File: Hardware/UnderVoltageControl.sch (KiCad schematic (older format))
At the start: 8 parts

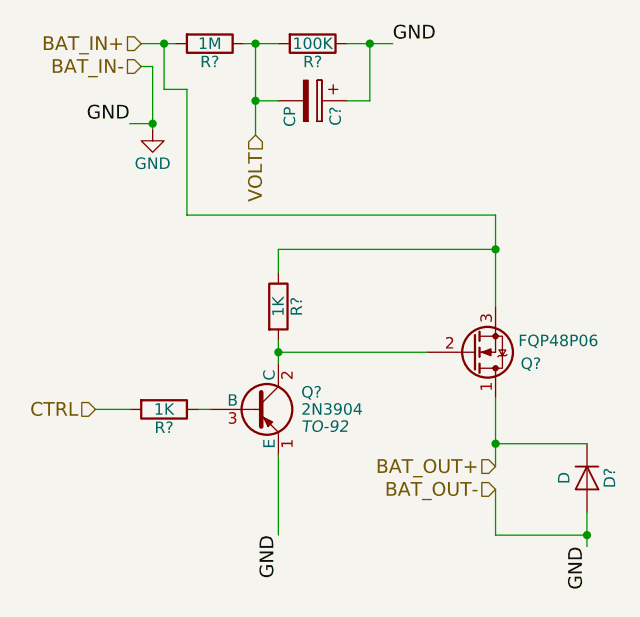
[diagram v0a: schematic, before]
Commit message: Add receiver component
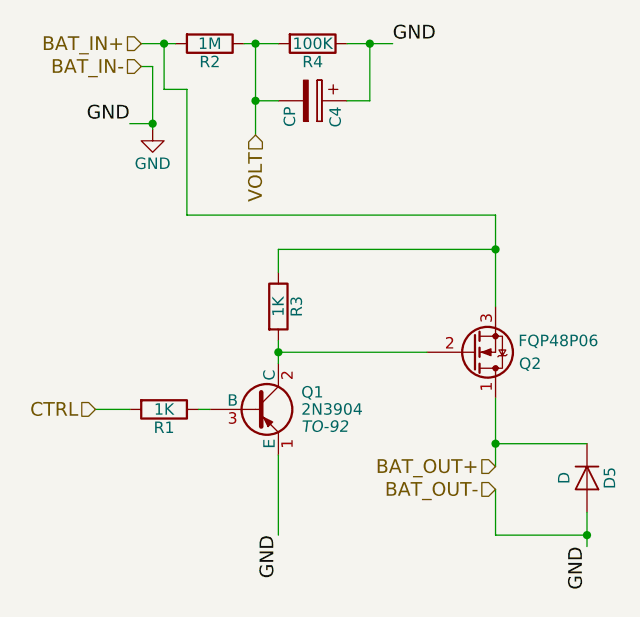
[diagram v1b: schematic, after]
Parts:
- gave numbers to parts that had none: 8
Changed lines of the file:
@@
 LIBS:valves
 LIBS:arduino
-LIBS:RC_Car_Manager-cache
+LIBS:RC_CAR
 EELAYER 25 0
 EELAYER END
@@
 $EndDescr
 $Comp
-L R R?
+L R R2
 U 1 1 5A34D119
 P 4775 2475
-F 0 "R?" V 4855 2475 50  0000 C CNN
+F 0 "R2" V 4855 2475 50  0000 C CNN
 F 1 "1M" V 4775 2475 50  0000 C CNN
 F 2 "" V 4705 2475 50  0000 C CNN
@@
 $EndComp
 $Comp
-L R R?
+L R R4
 U 1 1 5A34D120
 P 5225 2475
-F 0 "R?" V 5305 2475 50  0000 C CNN
+F 0 "R4" V 5305 2475 50  0000 C CNN
 F 1 "100K" V 5225 2475 50  0000 C CNN
 F 2 "" V 5155 2475 50  0000 C CNN
@@
 $EndComp
 $Comp
-L CP C?
+L CP C4
 U 1 1 5A34D127
 P 5225 2725
-F 0 "C?" H 5250 2825 50  0000 L CNN
+F 0 "C4" H 5250 2825 50  0000 L CNN
 F 1 "CP" H 5250 2625 50  0000 L CNN
 F 2 "" H 5263 2575 50  0000 C CNN
@@
 $EndComp
 $Comp
-L GND #PWR?
+L GND #PWR8
 U 1 1 5A34D12E
 P 4525 2850
-F 0 "#PWR?" H 4525 2600 50  0001 C CNN
+F 0 "#PWR8" H 4525 2600 50  0001 C CNN
 F 1 "GND" H 4525 2700 50  0000 C CNN
 F 2 "" H 4525 2850 50  0000 C CNN
@@
 Connection ~ 4975 2725
 $Comp
-L 2SA1016 Q?
+L 2SA1016 Q1
 U 1 1 5A34D145
 P 4975 4075
-F 0 "Q?" H 5175 4150 50  0000 L CNN
+F 0 "Q1" H 5175 4150 50  0000 L CNN
 F 1 "2N3904" H 5175 4075 50  0000 L CNN
 F 2 "TO-92" H 5175 4000 50  0000 L CIN
@@
 $EndComp
 $Comp
-L Q_NMOS_DGS Q?
+L Q_NMOS_DGS Q2
 U 1 1 5A34D14C
 P 5925 3825
-F 0 "Q?" H 6225 3875 50  0000 R CNN
+F 0 "Q2" H 6225 3875 50  0000 R CNN
 F 1 "FQP48P06" H 6475 3775 50  0000 R CNN
 F 2 "" H 6125 3925 50  0000 C CNN
@@
 	4675 3225 6025 3225
 $Comp
-L R R?
+L R R1
 U 1 1 5A34D15A
 P 4575 4075
-F 0 "R?" V 4655 4075 50  0000 C CNN
+F 0 "R1" V 4655 4075 50  0000 C CNN
 F 1 "1K" V 4575 4075 50  0000 C CNN
 F 2 "" V 4505 4075 50  0000 C CNN
@@
 $EndComp
 $Comp
-L R R?
+L R R3
 U 1 1 5A34D161
 P 5075 3625
-F 0 "R?" V 5155 3625 50  0000 C CNN
+F 0 "R3" V 5155 3625 50  0000 C CNN
 F 1 "1K" V 5075 3625 50  0000 C CNN
 F 2 "" V 5005 3625 50  0000 C CNN
@@
 	4425 4075 4275 4075
 $Comp
-L D D?
+L D D5
 U 1 1 5A34D172
 P 6425 4375
-F 0 "D?" H 6425 4475 50  0000 C CNN
+F 0 "D5" H 6425 4475 50  0000 C CNN
 F 1 "D" H 6425 4275 50  0000 C CNN
 F 2 "" H 6425 4375 50  0000 C CNN

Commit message: Resolves 2N3904 transistor miss match
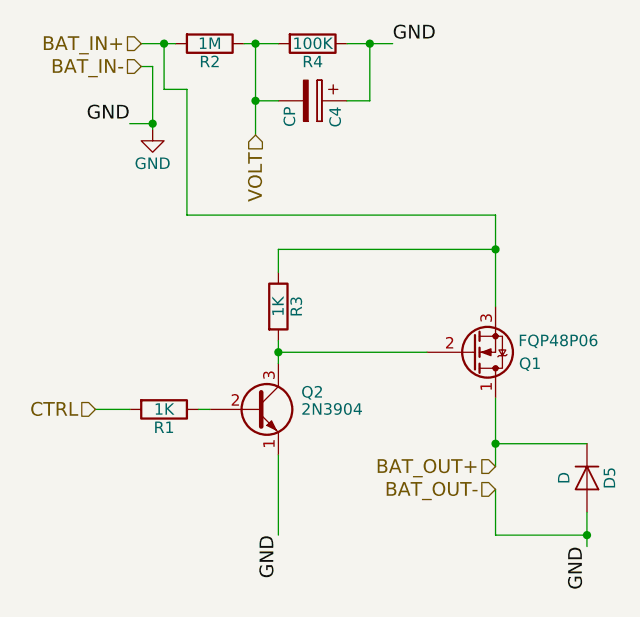
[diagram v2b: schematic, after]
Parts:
- removed Q1: 2N3904, TO-92, symbol 2SA1016
- added Q2: 2N3904, TO_SOT_Packages_THT:TO-92_Molded_Narrow, symbol 2N3904
- renumbered Q2 to Q1
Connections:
- net GND: now also Q2.1 (E)
- net at Q1.2 (G), R3.2: now also Q2.3 (C)
- net at R1.1: now also Q2.2 (B)
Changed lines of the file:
@@
 EESchema Schematic File Version 2
-LIBS:power
-LIBS:device
-LIBS:transistors
-LIBS:conn
-LIBS:linear
-LIBS:regul
-LIBS:74xx
-LIBS:cmos4000
-LIBS:adc-dac
-LIBS:memory
-LIBS:xilinx
-LIBS:microcontrollers
-LIBS:dsp
-LIBS:microchip
-LIBS:analog_switches
-LIBS:motorola
-LIBS:texas
-LIBS:intel
-LIBS:audio
-LIBS:interface
-LIBS:digital-audio
-LIBS:philips
-LIBS:display
-LIBS:cypress
-LIBS:siliconi
-LIBS:opto
-LIBS:atmel
-LIBS:contrib
-LIBS:valves
+LIBS:RC_Car_Manager-rescue
 LIBS:arduino
 LIBS:RC_CAR
+LIBS:74xgxx
+LIBS:74xx
+LIBS:ac-dc
+LIBS:actel
+LIBS:adc-dac
+LIBS:Altera
+LIBS:analog_devices
+LIBS:analog_switches
+LIBS:atmel
+LIBS:audio
+LIBS:battery_management
+LIBS:bbd
+LIBS:Bosch
+LIBS:brooktre
+LIBS:cmos_ieee
+LIBS:cmos4000
+LIBS:conn
+LIBS:Connector
+LIBS:contrib
+LIBS:cypress
+LIBS:dc-dc
+LIBS:Decawave
+LIBS:device
+LIBS:digital-audio
+LIBS:diode
+LIBS:display
+LIBS:driver_gate
+LIBS:dsp
+LIBS:DSP_Microchip_DSPIC33
+LIBS:elec-unifil
+LIBS:ESD_Protection
+LIBS:Espressif
+LIBS:FPGA_Actel
+LIBS:ftdi
+LIBS:gennum
+LIBS:graphic
+LIBS:hc11
+LIBS:infineon
+LIBS:intel
+LIBS:interface
+LIBS:intersil
+LIBS:ir
+LIBS:Lattice
+LIBS:LED
+LIBS:LEM
+LIBS:linear
+LIBS:Logic_74xgxx
+LIBS:Logic_74xx
+LIBS:Logic_CMOS_4000
+LIBS:Logic_CMOS_IEEE
+LIBS:logic_programmable
+LIBS:Logic_TTL_IEEE
+LIBS:logo
+LIBS:maxim
+LIBS:MCU_Microchip_PIC10
+LIBS:MCU_Microchip_PIC12
+LIBS:MCU_Microchip_PIC16
+LIBS:MCU_Microchip_PIC18
+LIBS:MCU_Microchip_PIC24
+LIBS:MCU_Microchip_PIC32
+LIBS:MCU_NXP_Kinetis
+LIBS:MCU_NXP_LPC
+LIBS:MCU_NXP_S08
+LIBS:MCU_Parallax
+LIBS:MCU_ST_STM8
+LIBS:MCU_ST_STM32
+LIBS:MCU_Texas_MSP430
+LIBS:Mechanical
+LIBS:memory
+LIBS:microchip
+LIBS:microchip_dspic33dsc
+LIBS:microchip_pic10mcu
+LIBS:microchip_pic12mcu
+LIBS:microchip_pic16mcu
+LIBS:microchip_pic18mcu
+LIBS:microchip_pic32mcu
+LIBS:microcontrollers
+LIBS:modules
+LIBS:Motor
+LIBS:motor_drivers
+LIBS:motorola
+LIBS:msp430
+LIBS:nordicsemi
+LIBS:nxp
+LIBS:nxp_armmcu
+LIBS:onsemi
+LIBS:opto
+LIBS:Oscillators
+LIBS:philips
+LIBS:power
+LIBS:Power_Management
+LIBS:powerint
+LIBS:pspice
+LIBS:references
+LIBS:regul
+LIBS:Relay
+LIBS:relays
+LIBS:RF_Bluetooth
+LIBS:rfcom
+LIBS:RFSolutions
+LIBS:Sensor_Current
+LIBS:Sensor_Humidity
+LIBS:sensors
+LIBS:silabs
+LIBS:siliconi
+LIBS:stm8
+LIBS:stm32
+LIBS:supertex
+LIBS:Switch
+LIBS:switches
+LIBS:texas
+LIBS:transf
+LIBS:Transformer
+LIBS:Transistor
+LIBS:transistors
+LIBS:triac_thyristor
+LIBS:ttl_ieee
+LIBS:Valve
+LIBS:valves
+LIBS:video
+LIBS:wiznet
+LIBS:Worldsemi
+LIBS:Xicor
+LIBS:xilinx
+LIBS:zetex
+LIBS:Zilog
+LIBS:RC_Car_Manager-cache
 EELAYER 25 0
 EELAYER END
@@
 $EndComp
 Wire Wire Line
-	4475 2475 4575 2475
-Wire Wire Line
-	4575 2475 4625 2475
-Wire Wire Line
-	4925 2475 4975 2475
-Wire Wire Line
-	4975 2475 5075 2475
-Wire Wire Line
-	5375 2475 5475 2475
-Wire Wire Line
-	5475 2475 5575 2475
+	4475 2475 4625 2475
+Wire Wire Line
+	4925 2475 5075 2475
+Wire Wire Line
+	5375 2475 5575 2475
 Wire Wire Line
 	5375 2725 5475 2725
@@
 	5075 2725 4975 2725
 Wire Wire Line
-	4975 2475 4975 2725
-Wire Wire Line
-	4975 2725 4975 2875
+	4975 2475 4975 2875
 Connection ~ 4975 2475
 Connection ~ 4975 2725
 $Comp
-L 2SA1016 Q1
-U 1 1 5A34D145
-P 4975 4075
-F 0 "Q1" H 5175 4150 50  0000 L CNN
-F 1 "2N3904" H 5175 4075 50  0000 L CNN
-F 2 "TO-92" H 5175 4000 50  0000 L CIN
-F 3 "" H 4975 4075 50  0000 L CNN
-	1    4975 4075
-	1    0    0    -1
-$EndComp
-$Comp
-L Q_NMOS_DGS Q2
+L Q_NMOS_DGS Q1
 U 1 1 5A34D14C
 P 5925 3825
-F 0 "Q2" H 6225 3875 50  0000 R CNN
+F 0 "Q1" H 6225 3875 50  0000 R CNN
 F 1 "FQP48P06" H 6475 3775 50  0000 R CNN
 F 2 "" H 6125 3925 50  0000 C CNN
@@
 $EndComp
 Wire Wire Line
-	4525 2850 4525 2825
-Wire Wire Line
-	4525 2825 4525 2575
+	4525 2575 4525 2850
 Wire Wire Line
 	4525 2575 4475 2575
@@
 $EndComp
 Wire Wire Line
-	6025 3225 6025 3375
-Wire Wire Line
-	6025 3375 6025 3625
+	6025 3225 6025 3625
 Wire Wire Line
 	6025 3375 5075 3375
@@
 Connection ~ 6025 3375
 Wire Wire Line
-	5075 3775 5075 3825
-Wire Wire Line
-	5075 3825 5075 3875
+	5075 3775 5075 3875
 Wire Wire Line
 	5725 3825 5075 3825
@@
 $EndComp
 Wire Wire Line
-	6025 4025 6025 4225
-Wire Wire Line
-	6025 4225 6025 4325
+	6025 4025 6025 4325
 Wire Wire Line
 	6025 4225 6425 4225
@@
 	5075 4275 5075 4625
 Wire Wire Line
-	6425 4525 6425 4625
-Wire Wire Line
-	6425 4625 6425 4675
+	6425 4525 6425 4675
 Wire Wire Line
 	6025 4425 6025 4625
@@
 Text HLabel 4975 2875 3    60   Input ~ 0
 VOLT
+$Comp
+L 2N3904 Q2
+U 1 1 5A33FE0E
+P 4975 4075
+F 0 "Q2" H 5175 4150 50  0000 L CNN
+F 1 "2N3904" H 5175 4075 50  0000 L CNN
+F 2 "TO_SOT_Packages_THT:TO-92_Molded_Narrow" H 5175 4000 50  0001 L CIN
+F 3 "" H 4975 4075 50  0001 L CNN
+	1    4975 4075
+	1    0    0    -1
+$EndComp
 $EndSCHEMATC
